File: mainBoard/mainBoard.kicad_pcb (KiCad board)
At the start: 4 copper layers, 110 x 75 mm, 74 parts, among them IC1 TCAN3414DR, J1 XT60PW-M, J10 RJ45, J11 RJ45, J12 Conn_01x03, J16 BM04B-SRSS-TB, J17 BM04B-SRSS-TB, J18 BM04B-SRSS-TB, J19 BM04B-SRSS-TB, J2 XT60PW-M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

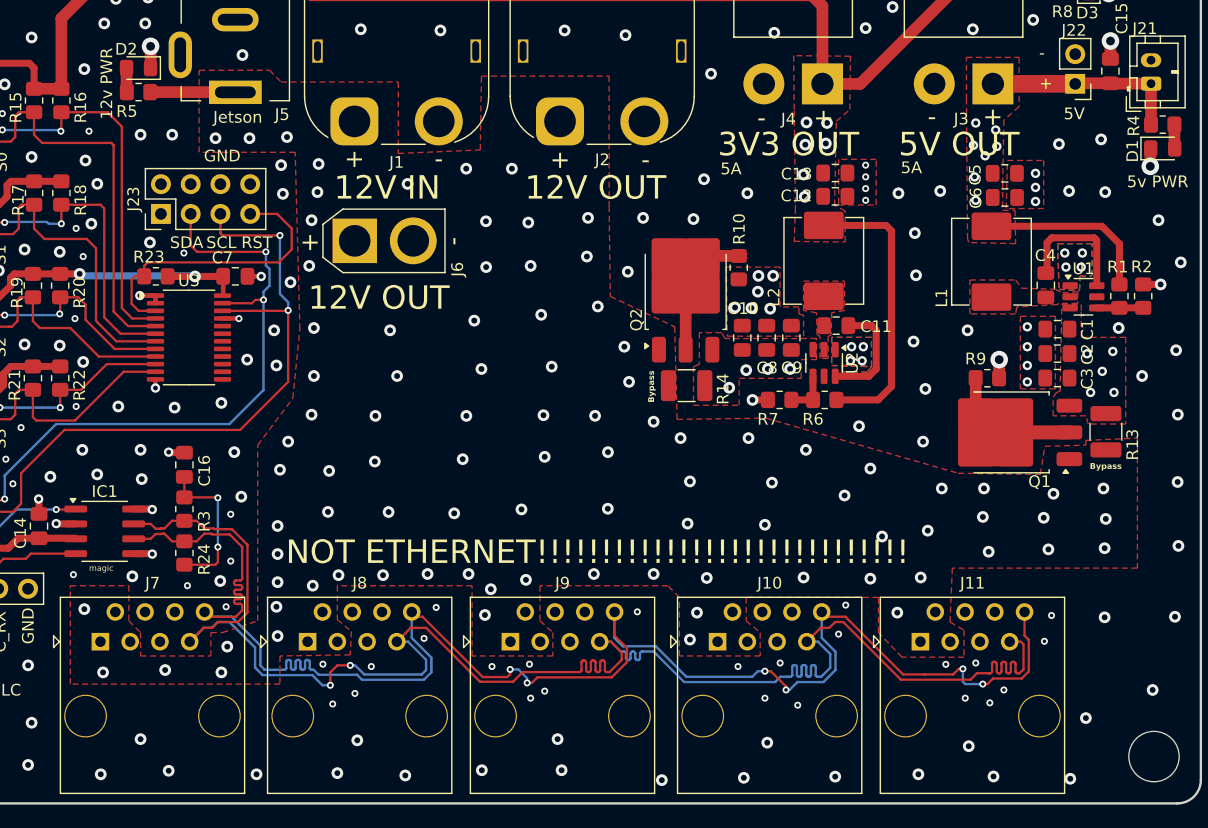
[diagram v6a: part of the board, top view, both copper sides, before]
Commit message: adjusted gap between rj45 ports
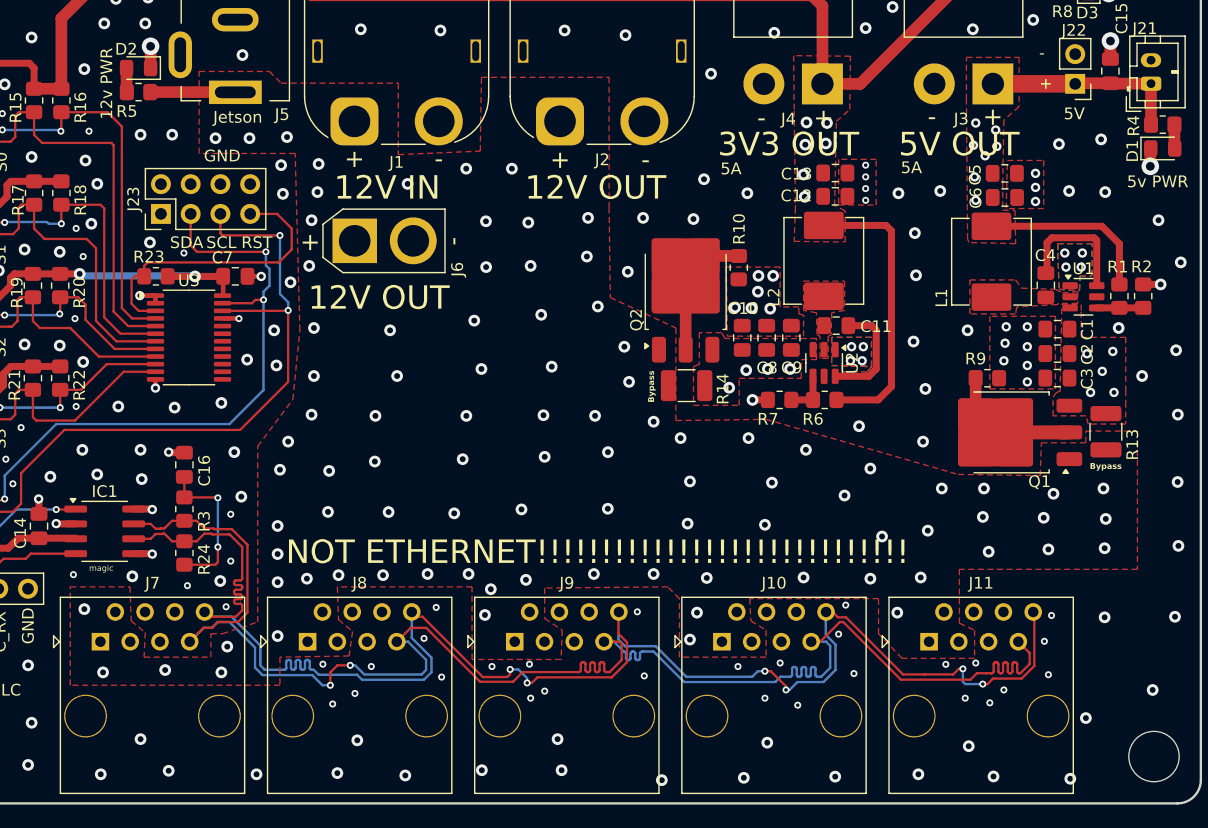
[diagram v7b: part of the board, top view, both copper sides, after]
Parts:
- moved J11 0.74 mm to (102.3, 81.0)
- moved J9 0.37 mm to (66.9, 81.0)
- moved J10 0.37 mm to (84.6, 81.0)
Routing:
- net CANN: track 140.2 -> 138.2 mm
- net CANP: track 145.5 -> 143.6 mm
- net GND: track 29.1 -> 27.5 mm, vias 202 -> 208
- net +12V: vias 93 -> 92

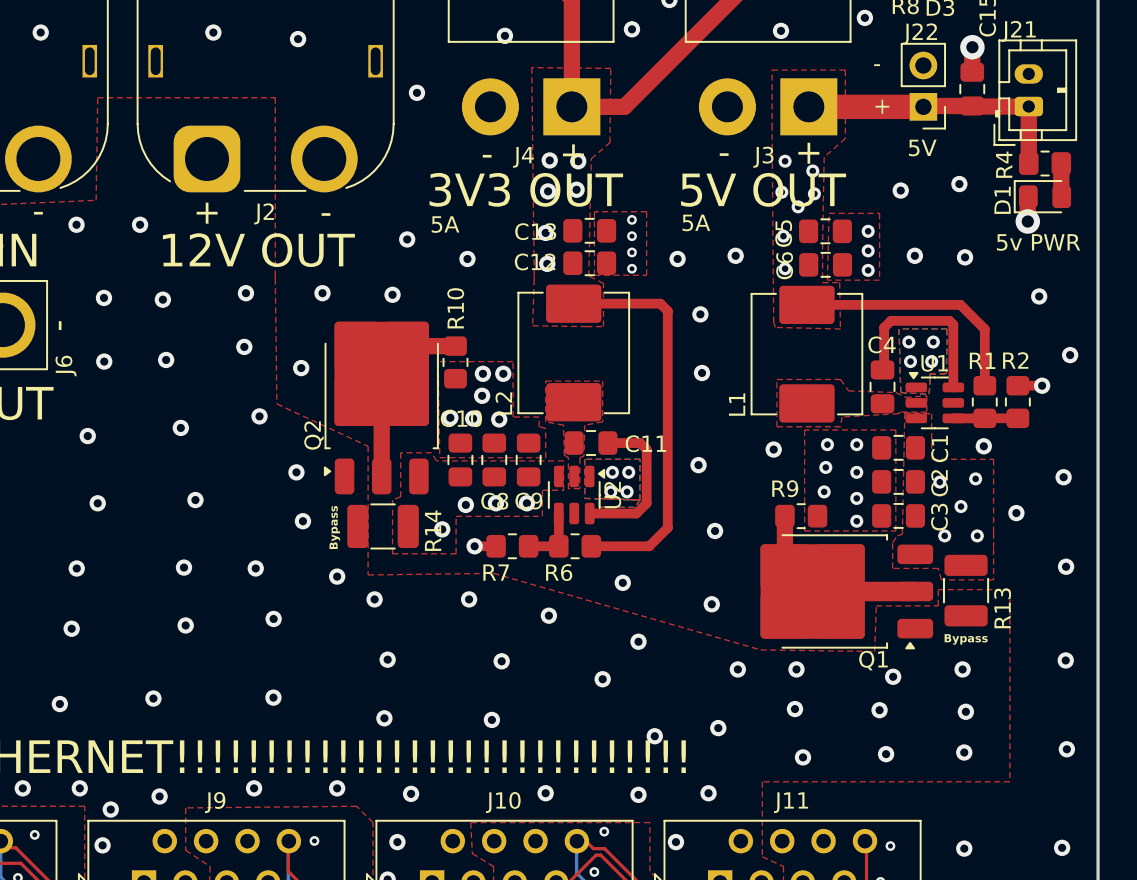
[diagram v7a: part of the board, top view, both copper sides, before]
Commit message: Fixed error with PNP mosfet
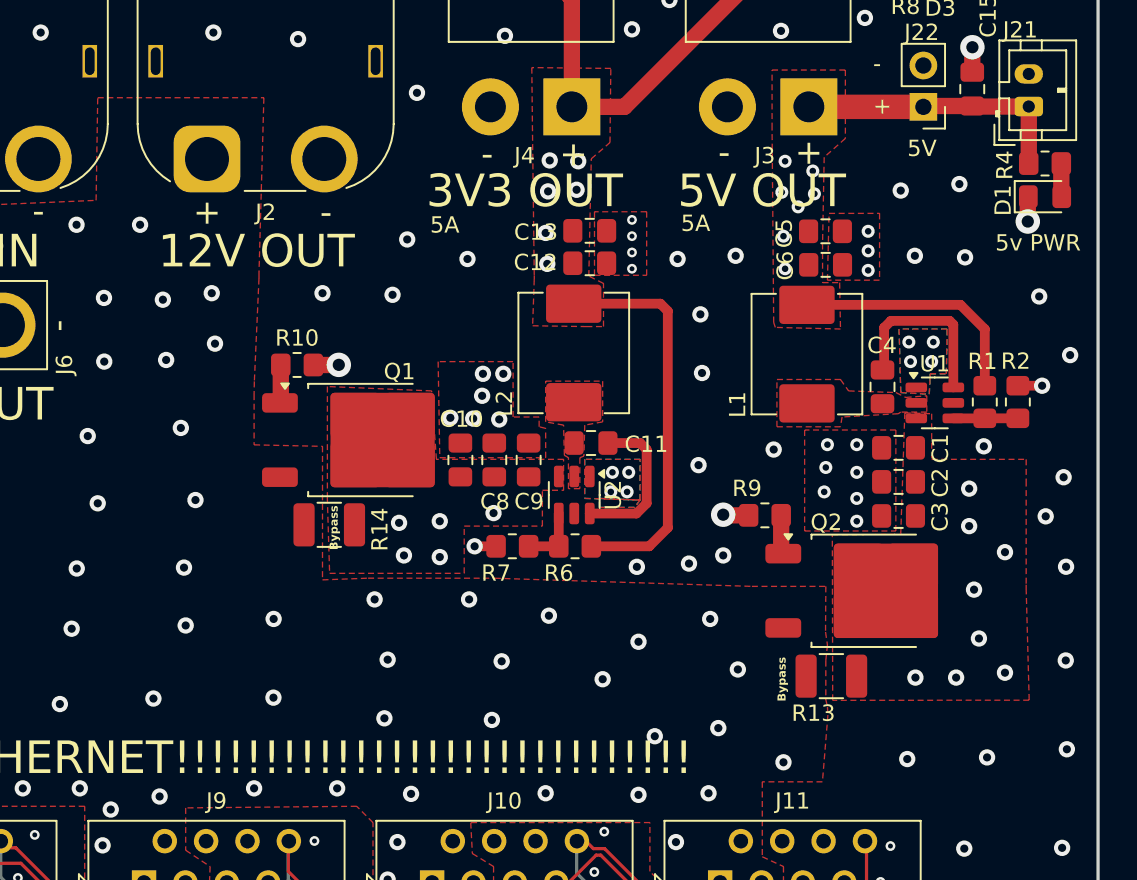
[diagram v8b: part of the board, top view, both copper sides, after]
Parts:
- Q1, Q2: footprint Package_TO_SOT_SMD:TO-252-3_TabPin2 -> Package_TO_SOT_SMD:TO-252-2
- moved Q2 32.0 mm to (111.2, 63.1), turned to 0 degrees
- moved Q1 30.4 mm to (80.3, 53.8), turned to 0 degrees
- moved R13 9.80 mm to (109.1, 68.3), turned to 180 degrees
- moved R10 9.73 mm to (76.3, 49.2), turned to 0 degrees
- moved R14 3.30 mm to (78.3, 59.0)
- moved R9 2.23 mm to (105.0, 58.5), turned to 180 degrees
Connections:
- C1 pad 1: Net-(Q1-S) -> Net-(Q2-S)
- C10 pad 1: Net-(Q2-S) -> Net-(Q1-S)
- C2 pad 1: Net-(Q1-S) -> Net-(Q2-S)
- C3 pad 1: Net-(Q1-S) -> Net-(Q2-S)
- C8 pad 1: Net-(Q2-S) -> Net-(Q1-S)
- C9 pad 1: Net-(Q2-S) -> Net-(Q1-S)
- Q1 pad 1: +12V -> Net-(Q1-G)
- Q1 pad 2: Net-(Q1-G) -> Net-(Q1-S)
- Q1 pad 3: Net-(Q1-S) -> +12V
- Q2 pad 1: +12V -> Net-(Q2-G)
- Q2 pad 2: Net-(Q2-G) -> Net-(Q2-S)
- Q2 pad 3: Net-(Q2-S) -> +12V
- R10 pad 1: Net-(Q2-G) -> Net-(Q1-G)
- R13 pad 1: Net-(Q1-S) -> Net-(Q2-S)
- R14 pad 1: Net-(Q2-S) -> Net-(Q1-S)
- R9 pad 1: Net-(Q1-G) -> Net-(Q2-G)
- U1 pad 3: Net-(Q1-S) -> Net-(Q2-S)
- U2 pad 3: Net-(Q2-S) -> Net-(Q1-S)
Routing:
- net Net-(Q1-G): track 9.37 -> 2.35 mm
- net Net-(Q2-G): track 9.28 -> 2.36 mm
- net GND: track 27.5 -> 30.6 mm, vias 208 -> 211
- net Net-(Q2-S): vias 4 -> 8
- net +12V: vias 92 -> 80
